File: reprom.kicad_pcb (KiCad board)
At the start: 2 copper layers, 44.4 x 40.6 mm, 14 parts, among them P1 KERNAL_SOCKET, P2 KERNAL_AND_BASIC_SOCKET, P3 LEFT_SOCKET, P4 RIGHT_SOCKET, P5 KERNAL, P6 CHARSET, P7 BASIC, U1 27512, U2 GAL16V8

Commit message: Hardware: Added additional pin headers for wider rom layouts (KU/326298)
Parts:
- added P8: LEFT_SOCKET_FAR, custom:Pin_Header_Straight_1x03, F.Cu at (114.3, 92.7)
- added P9: RIGHT_SOCKET_FAR, custom:Pin_Header_Straight_1x03, F.Cu at (165.1, 92.7)
- P3: value LEFT_SOCKET -> LEFT_SOCKET_CLOSE; footprint Pin_Headers:Pin_Header_Straight_2x03 -> custom:Pin_Header_Straight_2x03
- P4: value RIGHT_SOCKET -> RIGHT_SOCKET_CLOSE; footprint Pin_Headers:Pin_Header_Straight_1x03 -> custom:Pin_Header_Straight_1x03
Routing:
- net /BCS: track 28.5 -> 33.7 mm
- net /CS: track 66.9 -> 71.9 mm
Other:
- board size 44.4 x 40.6 mm -> 54.4 x 40.6 mm

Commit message: Revert "Hardware: Added additional pin headers for wider rom layouts (KU/326298)"
This reverts commit 2e8d7ef8814329ef0b47112793623fe7f19c62f6.
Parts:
- removed P8: LEFT_SOCKET_FAR, custom:Pin_Header_Straight_1x03
- removed P9: RIGHT_SOCKET_FAR, custom:Pin_Header_Straight_1x03
- P3: value LEFT_SOCKET_CLOSE -> LEFT_SOCKET; footprint custom:Pin_Header_Straight_2x03 -> Pin_Headers:Pin_Header_Straight_2x03
- P4: value RIGHT_SOCKET_CLOSE -> RIGHT_SOCKET; footprint custom:Pin_Header_Straight_1x03 -> Pin_Headers:Pin_Header_Straight_1x03
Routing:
- net /BCS: track 33.7 -> 28.5 mm
- net /CS: track 71.9 -> 66.9 mm
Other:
- board size 54.4 x 40.6 mm -> 44.4 x 40.6 mm

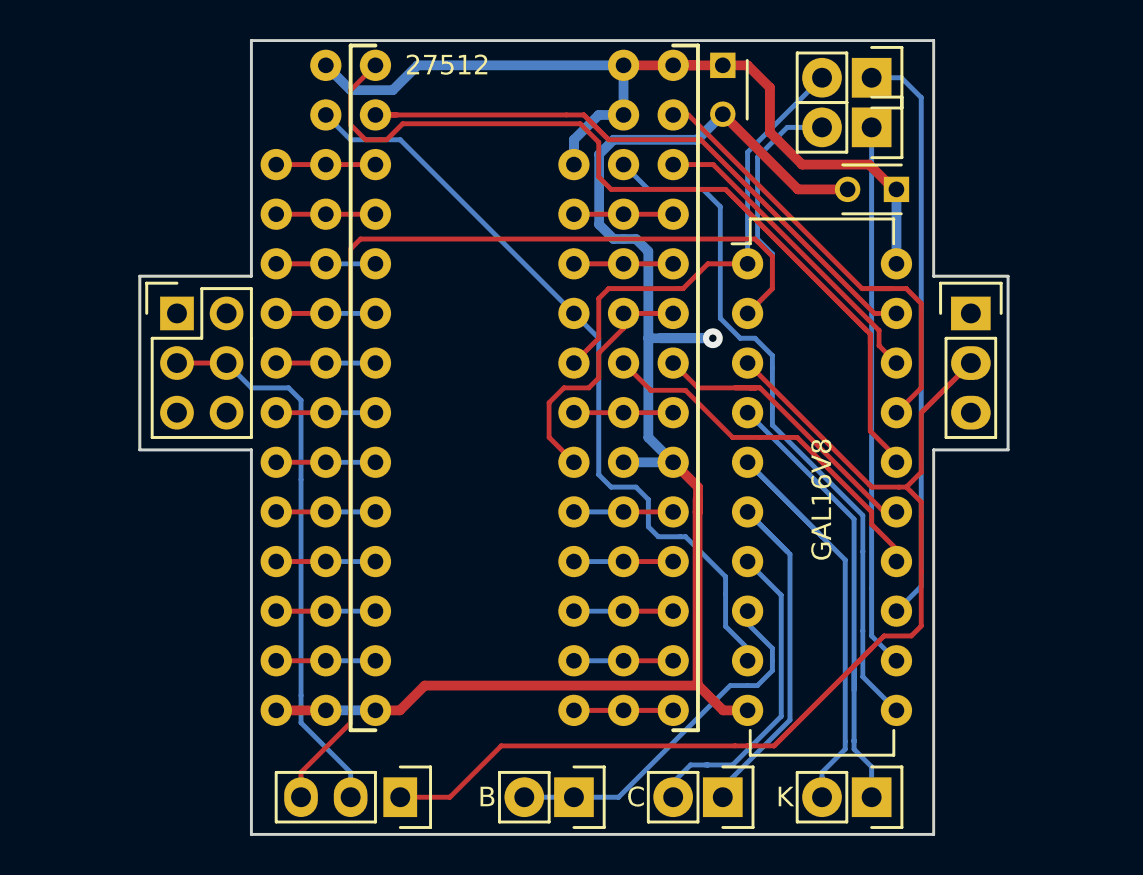
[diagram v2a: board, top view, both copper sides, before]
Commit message: Hardware: Added support for all board types
This adds the pin headers required to use the adapter
on ancient boards (396298 and KU14194HB) and on the
SX64 CPU board (251102).
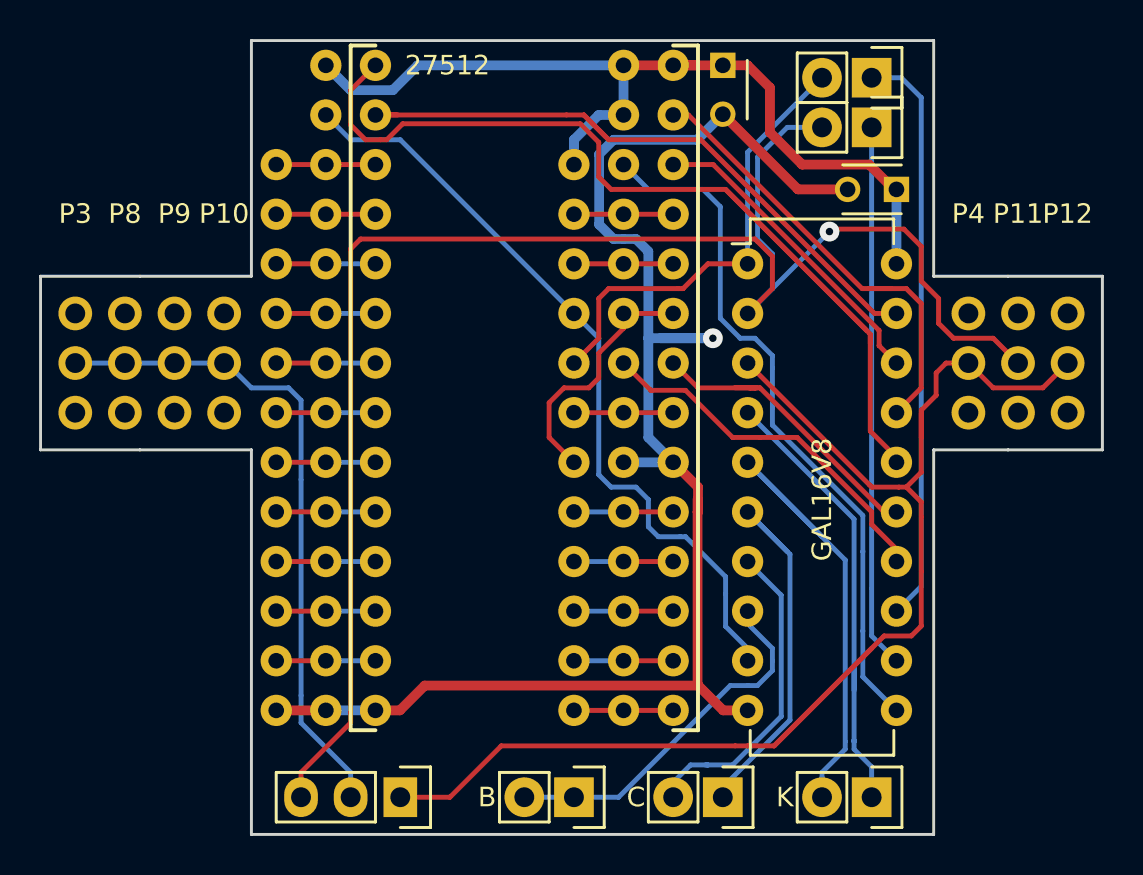
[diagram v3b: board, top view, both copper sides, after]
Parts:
- added P10: NEW_LEFT, custom:Pin_Header_Straight_1x03, F.Cu at (121.9, 92.7)
- added P11: SX64_RIGHT, custom:Pin_Header_Straight_1x03, F.Cu at (162.6, 92.7)
- added P12: ANCIENT_RIGHT, custom:Pin_Header_Straight_1x03, F.Cu at (165.1, 92.7)
- added P8: SX64_LEFT, custom:Pin_Header_Straight_1x03, F.Cu at (116.8, 92.7)
- added P9: OLD_LEFT, custom:Pin_Header_Straight_1x03, F.Cu at (119.4, 92.7)
- P3: value LEFT_SOCKET -> ANCIENT_LEFT; footprint Pin_Headers:Pin_Header_Straight_2x03 -> custom:Pin_Header_Straight_1x03
- P4: value RIGHT_SOCKET -> OLD_RIGHT; footprint Pin_Headers:Pin_Header_Straight_1x03 -> custom:Pin_Header_Straight_1x03
- moved P3 5.21 mm to (114.3, 92.7)
- moved P4 0.13 mm to (160.0, 92.7)
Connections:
- P3 pad 2: Net-(P3-Pad2) -> /BCS
- P3 pad 3: /BCS -> Net-(P3-Pad3)
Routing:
- net /BS: track 67.6 -> 87.9 mm, vias 0 -> 1
- net /BCS: track 28.5 -> 33.6 mm
- net /CS: track 66.9 -> 71.4 mm
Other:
- board size 44.4 x 40.6 mm -> 54.4 x 40.6 mm

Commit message: Hardware: Improved silkscreen, added board rev info
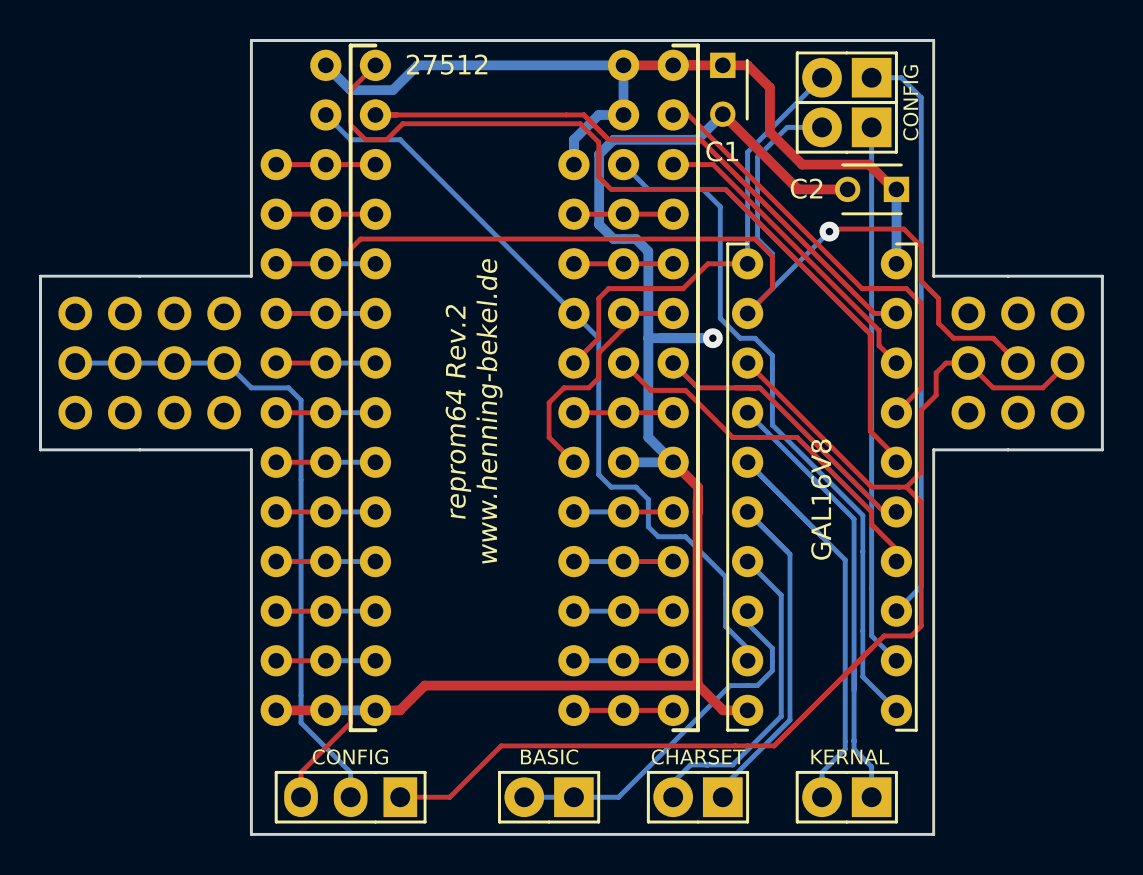
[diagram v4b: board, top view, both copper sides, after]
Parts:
- JP1: footprint Pin_Headers:Pin_Header_Straight_1x03 -> custom:Pin_Header_Straight_1x03_simple
- JP2, JP3, P5, P6, P7: footprint Pin_Headers:Pin_Header_Straight_1x02 -> custom:Pin_Header_Straight_1x02
- U2: footprint Housings_DIP:DIP-20_W7.62mm -> custom:DIP-20_W7.62mm
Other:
- board text added: "BASIC"
- board text added: "CHARSET"
- board text added: "CONFIG"
- board text added: "KERNAL"
- board text added: "reprom64 Rev.2 www.henning-bekel.de"
- board text removed: "B"
- board text removed: "C"
- board text removed: "K"
